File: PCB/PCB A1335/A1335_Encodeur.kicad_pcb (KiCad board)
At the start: 2 copper layers, 13 parts, among them P1 CONN_01X04, Q1 MOS_N, Q2 MOS_N, U1 662K, U2 A1335LLETR-T

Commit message: A1335_upload_files
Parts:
- removed R3, R4, R5, R6: 0, R_1206
- added W1: 0, TESTPT, B.Cu at (129.4, 105.4)
- added W2: 0, TESTPT, B.Cu at (125.1, 105.4)
- added W3: 0, TESTPT, B.Cu at (129.4, 107.3)
- added W4: 0, TESTPT, B.Cu at (125.1, 107.3)
- C1, C2: footprint C_1206 -> C_0805_HandSoldering
- Q1, Q2: value MOS_N -> BSS138
- R1, R2: footprint R_1206 -> R_0805_HandSoldering
- moved Q2 7.37 mm to (129.2, 111.6)
- moved U1 6.50 mm to (123.2, 111.6)
- moved P1 6.48 mm to (122.6, 114.9), turned to 270 degrees
- moved R1 3.88 mm to (129.0, 111.0), turned to 0 degrees
- moved R2 3.15 mm to (124.3, 111.0), turned to 180 degrees
- moved C1 2.55 mm to (127.0, 112.8), turned to 0 degrees
- moved Q1 1.49 mm to (126.2, 111.6)
- moved C2 1.42 mm to (122.6, 106.7), turned to 90 degrees
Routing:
- net GND: track 0.00 -> 18.6 mm, vias 0 -> 5
- net +3.3V: track 0.00 -> 15.2 mm, vias 0 -> 2
- net Net-(C2-Pad1): track 0.00 -> 11.2 mm, vias 0 -> 1
- net /SCL_33: track 0.00 -> 11.0 mm, vias 0 -> 1
- net +5V: track 0.00 -> 9.11 mm, vias 0 -> 1
- net /SDA_33: track 0.00 -> 5.79 mm, vias 0 -> 1
- net Net-(U2-Pad13): track 0.00 -> 4.54 mm, vias 0 -> 1
- net Net-(U2-Pad12): track 0.00 -> 4.53 mm, vias 0 -> 1
- net /SCL: track 0.00 -> 2.45 mm
- net /SDA: track 0.00 -> 2.33 mm
- added copper zone on B.Cu, net GND
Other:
- net class ALIM added: clearance 0.2, trace_width 0.4, via_dia 0.6, via_drill 0.4

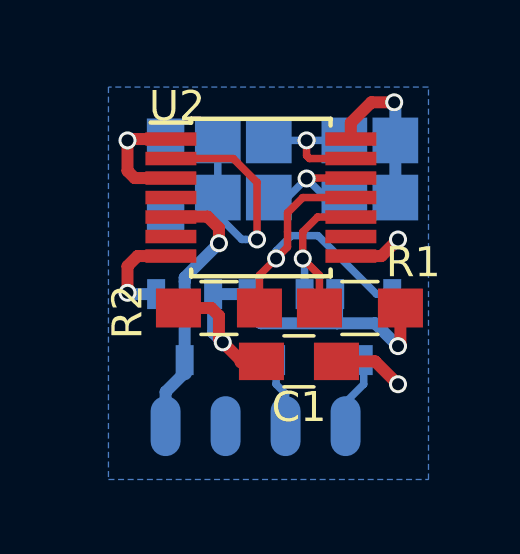
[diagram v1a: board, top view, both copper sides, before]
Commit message: Update-pcb-resistance-position
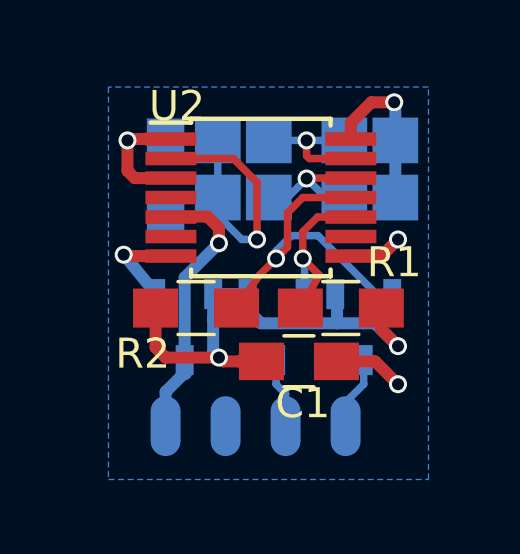
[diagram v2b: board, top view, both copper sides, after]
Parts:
- moved R2 0.76 mm to (123.6, 111.0)
- moved R1 0.64 mm to (128.4, 111.0)
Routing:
- net +3.3V: track 15.2 -> 18.7 mm
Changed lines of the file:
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@@
     (links 30)
     (no_connects 0)
-    (area 116.88 103.150999 141.072999 121.88)
+    (area 108.514287 99.408 141.072999 121.88)
     (thickness 1.6)
-    (drawings 11)
-    (tracks 113)
+    (drawings 13)
+    (tracks 115)
     (zones 0)
     (modules 13)
@@
   )
   (layers
-    (0 F.Cu signal hide)
-    (31 B.Cu signal hide)
+    (0 F.Cu signal)
+    (31 B.Cu signal)
     (32 B.Adhes user hide)
     (33 F.Adhes user hide)
     (34 B.Paste user hide)
     (35 F.Paste user hide)
-    (36 B.SilkS user)
+    (36 B.SilkS user hide)
     (37 F.SilkS user hide)
     (38 B.Mask user hide)
@@
     (46 B.CrtYd user hide)
     (47 F.CrtYd user hide)
-    (48 B.Fab user hide)
+    (48 B.Fab user)
     (49 F.Fab user)
   )
@@
     (aux_axis_origin 120.269 117.094)
     (grid_origin 120.269 117.094)
-    (visible_elements 7FFF7FBF)
+    (visible_elements 7FFEFFFF)
     (pcbplotparams
-      (layerselection 0x00000_00000000)
+      (layerselection 0x3c0ff_80000001)
       (usegerberextensions false)
-      (excludeedgelayer false)
+      (excludeedgelayer true)
       (linewidth 0.100000)
       (plotframeref false)
@@
       (padsonsilk false)
       (subtractmaskfromsilk false)
-      (outputformat 4)
-      (mirror true)
+      (outputformat 1)
+      (mirror false)
       (drillshape 0)
       (scaleselection 1)
@@
     (tags "capacitor 0805")
     (attr smd)
-    (fp_text reference C1 (at 0 1.524) (layer F.SilkS)
+    (fp_text reference C1 (at 0.127 1.397) (layer F.SilkS)
       (effects (font (size 1 1) (thickness 0.15)))
     )
@@
       (effects (font (size 1 1) (thickness 0.15)))
     )
-    (fp_text user C1 (at -2.032 0) (layer F.Fab)
-      (effects (font (size 1 1) (thickness 0.15)))
-    )
-    (fp_text user %R (at 0 -1.75) (layer F.Fab)
-      (effects (font (size 1 1) (thickness 0.15)))
+    (fp_text user C1 (at 0 0) (layer F.Fab)
+      (effects (font (size 0.8 0.8) (thickness 0.15)))
     )
     (fp_line (start -1 0.62) (end -1 -0.62) (layer F.Fab) (width 0.1))
@@
   )
   (module R_0805_HandSoldering (layer F.Cu)
-    (at 129.032 110.998)
+    (at 128.397 110.998)
     (descr "Resistor SMD 0805, hand soldering")
     (tags "resistor 0805")
@@
   )
   (module R_0805_HandSoldering (layer F.Cu)
-    (at 124.333 110.998 180)
+    (at 123.571 110.998 180)
     (descr "Resistor SMD 0805, hand soldering")
     (tags "resistor 0805")
     (attr smd)
-    (fp_text reference R2 (at 3.048 -0.127 270) (layer F.SilkS)
+    (fp_text reference R2 (at 1.778 -1.524 360) (layer F.SilkS)
       (effects (font (size 1 1) (thickness 0.15)))
     )
@@
     )
   )
+  (dimension 4.97 (width 0.3) (layer B.Fab)
+    (gr_text "4,970 mm" (at 117.879 114.864 90) (layer B.Fab)
+      (effects (font (size 1.5 1.5) (thickness 0.3)))
+    )
+    (feature1 (pts (xy 125.459 103.254) (xy 115.489 103.254)))
+    (feature2 (pts (xy 125.459 108.224) (xy 115.489 108.224)))
+    (crossbar (pts (xy 118.189 108.224) (xy 118.189 103.254)))
+    (arrow1a (pts (xy 118.189 103.254) (xy 118.775421 104.380504)))
+    (arrow1b (pts (xy 118.189 103.254) (xy 117.602579 104.380504)))
+    (arrow2a (pts (xy 118.189 108.224) (xy 118.775421 107.097496)))
+    (arrow2b (pts (xy 118.189 108.224) (xy 117.602579 107.097496)))
+  )
+  (dimension 5.461 (width 0.3) (layer B.Fab)
+    (gr_text "5,461 mm" (at 114.3 100.711) (layer B.Fab)
+      (effects (font (size 1.5 1.5) (thickness 0.3)))
+    )
+    (feature1 (pts (xy 120.269 107.95) (xy 120.269 99.408)))
+    (feature2 (pts (xy 125.73 107.95) (xy 125.73 99.408)))
+    (crossbar (pts (xy 125.73 102.108) (xy 120.269 102.108)))
+    (arrow1a (pts (xy 120.269 102.108) (xy 121.395504 101.521579)))
+    (arrow1b (pts (xy 120.269 102.108) (xy 121.395504 102.694421)))
+    (arrow2a (pts (xy 125.73 102.108) (xy 124.603496 101.521579)))
+    (arrow2b (pts (xy 125.73 102.108) (xy 124.603496 102.694421)))
+  )
   (gr_line (start 131.699 117.094) (end 131.699 103.251) (angle 90) (layer B.Fab) (width 0.2))
   (gr_line (start 120.269 117.094) (end 131.699 117.094) (angle 90) (layer B.Fab) (width 0.2))
@@
   (gr_line (start 131.699 103.251) (end 120.269 103.251) (angle 90) (layer F.Fab) (width 0.2))
   (target plus (at 119.38 119.38) (size 5) (width 0.15) (layer Edge.Cuts))
+  (segment (start 124.333 112.649) (end 122.555 112.649) (width 0.4) (layer F.Cu) (net 1))
+  (segment (start 122.221 112.315) (end 122.221 110.998) (width 0.4) (layer F.Cu) (net 1))
+  (segment (start 122.555 112.649) (end 122.221 112.315) (width 0.4) (layer F.Cu) (net 1))
+  (segment (start 129.747 110.998) (end 129.747 111.713) (width 0.4) (layer F.Cu) (net 1))
+  (segment (start 129.747 111.713) (end 130.302 112.268) (width 0.4) (layer F.Cu) (net 1))
+  (segment (start 129.159 111.506) (end 129.54 111.506) (width 0.4) (layer B.Cu) (net 1))
+  (segment (start 129.54 111.506) (end 130.302 112.268) (width 0.4) (layer B.Cu) (net 1))
+  (segment (start 125.75 112.776) (end 124.46 112.776) (width 0.4) (layer F.Cu) (net 1))
+  (segment (start 124.46 112.776) (end 124.333 112.649) (width 0.4) (layer F.Cu) (net 1))
+  (segment (start 124.14 111.379) (end 124.14 112.456) (width 0.4) (layer B.Cu) (net 1))
+  (via (at 124.333 112.649) (size 0.6) (drill 0.4) (layers F.Cu B.Cu) (net 1))
+  (segment (start 124.14 110.533) (end 124.14 111.379) (width 0.4) (layer B.Cu) (net 1))
+  (segment (start 124.14 112.456) (end 124.333 112.649) (width 0.4) (layer B.Cu) (net 1))
   (segment (start 125.75 112.776) (end 125.095 112.776) (width 0.5) (layer F.Cu) (net 1))
-  (segment (start 125.095 112.776) (end 124.46 112.141) (width 0.4) (layer F.Cu) (net 1))
   (segment (start 128.27 111.506) (end 128.27 110.594) (width 0.4) (layer B.Cu) (net 1))
   (segment (start 128.27 110.594) (end 128.209 110.533) (width 0.25) (layer B.Cu) (net 1))
@@
   (segment (start 125.73 111.506) (end 128.27 111.506) (width 0.4) (layer B.Cu) (net 1))
   (segment (start 125.288 111.064) (end 125.73 111.506) (width 0.4) (layer B.Cu) (net 1))
-  (segment (start 130.382 112.188) (end 130.382 110.998) (width 0.4) (layer F.Cu) (net 1))
-  (segment (start 128.27 111.506) (end 129.54 111.506) (width 0.4) (layer B.Cu) (net 1))
+  (segment (start 128.27 111.506) (end 129.159 111.506) (width 0.4) (layer B.Cu) (net 1))
   (segment (start 129.54 111.506) (end 130.302 112.268) (width 0.4) (layer B.Cu) (net 1))
   (via (at 130.302 112.268) (size 0.6) (drill 0.4) (layers F.Cu B.Cu) (net 1))
-  (segment (start 130.302 112.268) (end 130.382 112.188) (width 0.4) (layer F.Cu) (net 1))
-  (segment (start 124.14 110.533) (end 124.14 111.821) (width 0.4) (layer B.Cu) (net 1))
-  (via (at 124.46 112.141) (size 0.6) (drill 0.4) (layers F.Cu B.Cu) (net 1))
-  (segment (start 124.14 111.821) (end 124.46 112.141) (width 0.4) (layer B.Cu) (net 1))
-  (segment (start 124.46 112.141) (end 124.333 112.014) (width 0.4) (layer F.Cu) (net 1))
-  (segment (start 124.079 110.998) (end 122.983 110.998) (width 0.4) (layer F.Cu) (net 1))
-  (segment (start 124.333 111.252) (end 124.079 110.998) (width 0.4) (layer F.Cu) (net 1))
-  (segment (start 124.333 112.014) (end 124.333 111.252) (width 0.4) (layer F.Cu) (net 1))
   (segment (start 124.14 110.533) (end 125.288 110.533) (width 0.4) (layer B.Cu) (net 1))
-  (segment (start 122.73 109.265) (end 121.621 109.265) (width 0.4) (layer F.Cu) (net 2))
-  (segment (start 121.328 110.533) (end 121.285 110.49) (width 0.4) (layer B.Cu) (net 2))
-  (via (at 121.285 110.49) (size 0.6) (drill 0.4) (layers F.Cu B.Cu) (net 2))
-  (segment (start 121.328 110.533) (end 122.24 110.533) (width 0.4) (layer B.Cu) (net 2))
-  (segment (start 121.285 109.601) (end 121.285 110.49) (width 0.4) (layer F.Cu) (net 2))
-  (segment (start 121.621 109.265) (end 121.285 109.601) (width 0.4) (layer F.Cu) (net 2))
+  (segment (start 122.73 109.265) (end 121.203 109.265) (width 0.4) (layer F.Cu) (net 2))
+  (segment (start 121.203 109.265) (end 121.158 109.22) (width 0.4) (layer F.Cu) (net 2))
+  (segment (start 121.201 109.263) (end 121.158 109.22) (width 0.4) (layer B.Cu) (net 2))
+  (segment (start 121.201 109.263) (end 122.24 110.533) (width 0.4) (layer B.Cu) (net 2))
+  (via (at 121.158 109.22) (size 0.6) (drill 0.4) (layers F.Cu B.Cu) (net 2))
   (segment (start 128.25 112.776) (end 129.54 112.776) (width 0.4) (layer F.Cu) (net 2))
   (segment (start 129.54 112.776) (end 130.302 113.538) (width 0.4) (layer F.Cu) (net 2))
@@
   (segment (start 123.17 107.315) (end 124.2949 107.315) (width 0.25) (layer B.Cu) (net 3))
   (segment (start 124.2949 107.315) (end 124.2949 105.41) (width 0.25) (layer B.Cu) (net 3))
-  (segment (start 127.682 110.998) (end 127.682 109.902) (width 0.25) (layer F.Cu) (net 4))
+  (segment (start 127.047 110.998) (end 127.682 109.902) (width 0.25) (layer F.Cu) (net 4) (status 10))
   (segment (start 127.682 109.902) (end 127.127 109.347) (width 0.25) (layer F.Cu) (net 4))
   (segment (start 127.188 110.533) (end 127.188 109.408) (width 0.25) (layer B.Cu) (net 4))
@@
   (segment (start 128.397 109.347) (end 127.635 108.585) (width 0.25) (layer B.Cu) (net 5))
   (segment (start 129.583 110.533) (end 128.397 109.347) (width 0.25) (layer B.Cu) (net 5))
-  (segment (start 125.683 110.998) (end 125.683 109.902) (width 0.25) (layer F.Cu) (net 5))
+  (segment (start 124.921 110.998) (end 125.683 109.902) (width 0.25) (layer F.Cu) (net 5) (status 10))
   (segment (start 125.683 109.902) (end 126.238 109.347) (width 0.25) (layer F.Cu) (net 5))
   (segment (start 126.238 109.347) (end 126.238 109.093) (width 0.25) (layer B.Cu) (net 5))
